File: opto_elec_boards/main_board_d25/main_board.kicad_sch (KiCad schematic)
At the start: 28 parts, among them J1 IN1_BNC, J10 To Slave Board, J11 SWITCH_B, J12 SWITCH_C, J13 DB25_Socket_MountingHoles, J2 IN2_BNC, J3 OUT1_BNC, J4 OUT2_BNC, J5 OUT3_BNC, J6 OUT4_BNC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

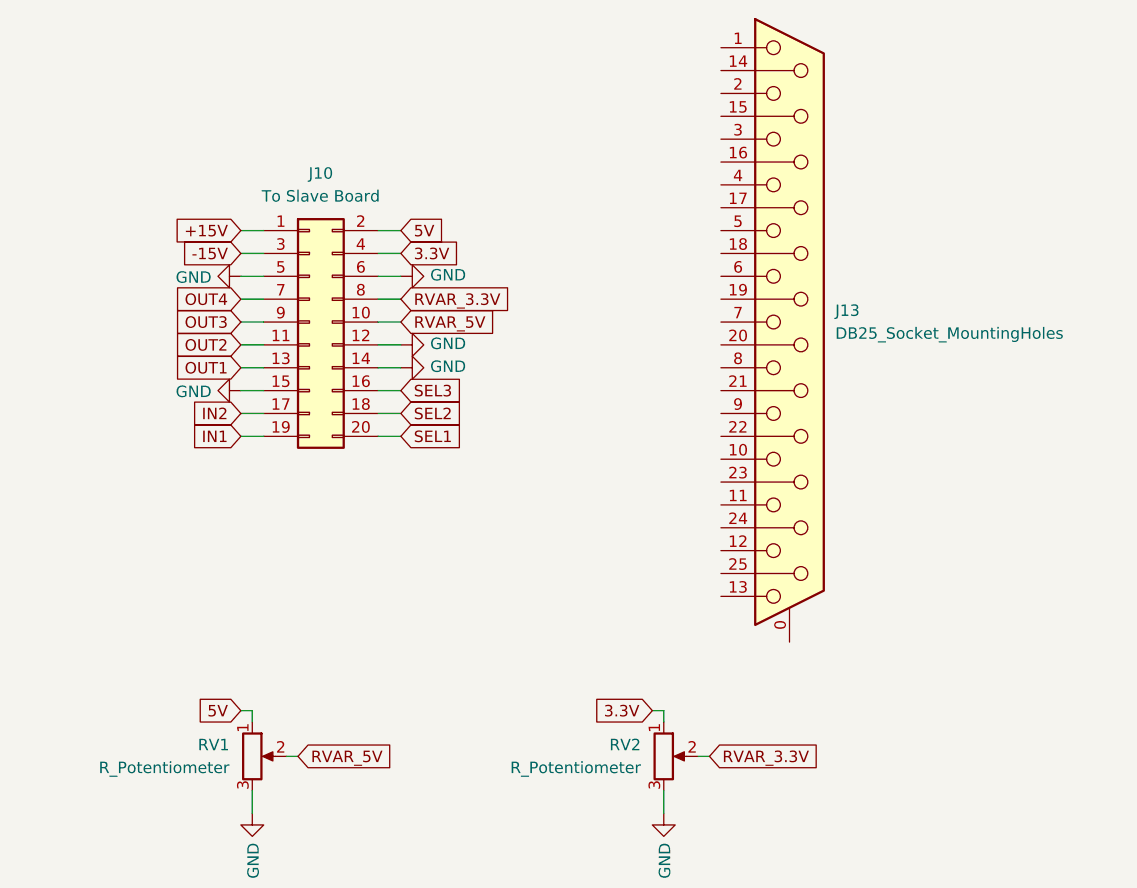
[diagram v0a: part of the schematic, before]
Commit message: Create Opto Board Main D25 / new connector test
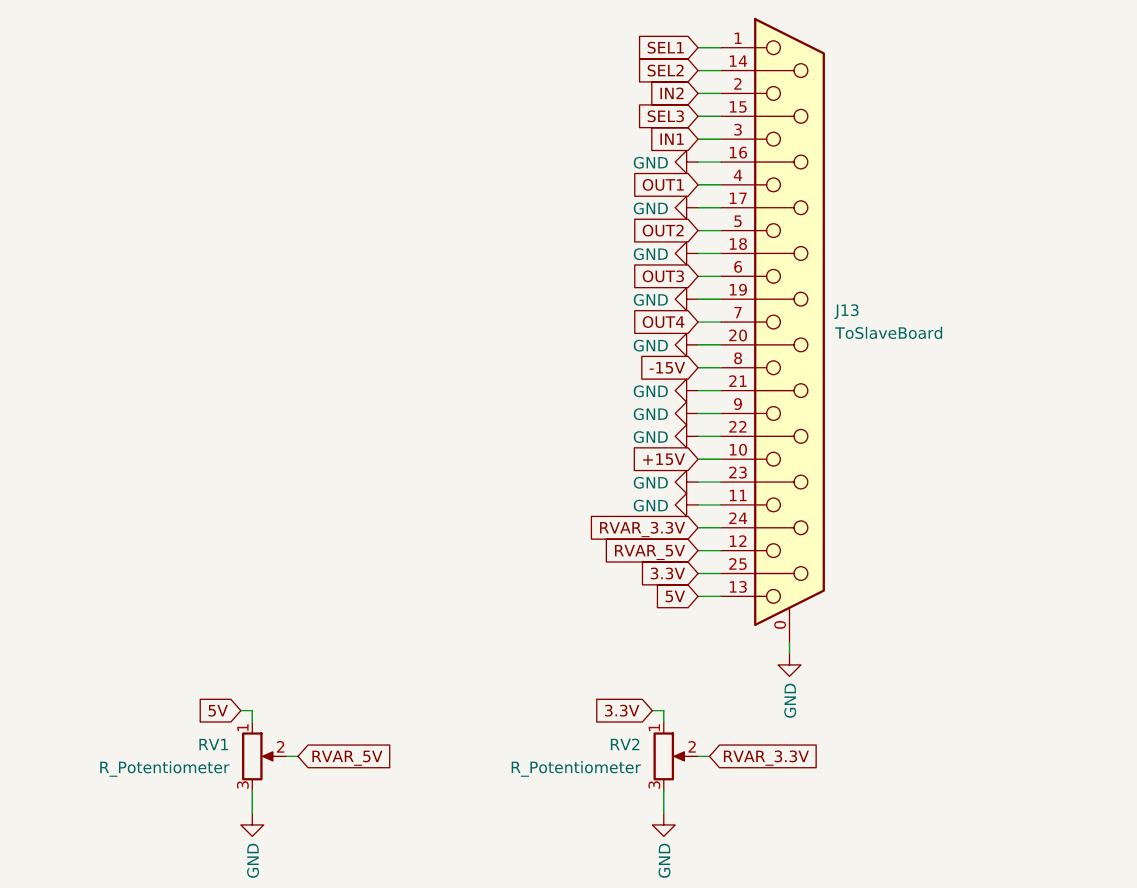
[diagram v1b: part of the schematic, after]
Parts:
- removed J10: To Slave Board, Connector_PinSocket_2.54mm:PinSocket_2x10_P2.54mm_Horizontal, symbol Connector_Generic:Conn_02x10_Odd_Even
- J13: value DB25_Socket_MountingHoles -> ToSlaveBoard
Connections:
- net +15V: now also J13.10
- net -15V: now also J13.8
- net 3.3V: now also J13.25 (P25)
- net 5V: now also J13.13
- net GND: now also J13.0 (PAD), J13.11, J13.16 (P16), J13.17 (P17), J13.18 (P18), J13.19 (P19), J13.20 (P20), J13.21 (P21), J13.22 (P22), J13.23 (P23), J13.9
- net IN1: now also J13.3
- net IN2: now also J13.2
- net OUT1: now also J13.4
- net OUT2: now also J13.5
- net OUT3: now also J13.6
- net OUT4: now also J13.7
- net RVAR_3.3V: now also J13.24 (P24)
- net RVAR_5V: now also J13.12
- net SEL1: now also J13.1
- net SEL2: now also J13.14 (P14)
- net SEL3: now also J13.15 (P15)

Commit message: Update OptoBoard / D25 version
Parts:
- added RV3: R_Potentiometer, Connector_PinHeader_2.54mm:PinHeader_1x03_P2.54mm_Vertical, symbol Device:R_Potentiometer
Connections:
- net +15V: now also RV3.1
- net GND: now also RV3.3; no longer J13.11
- new net RVAR_15V: J13.11, RV3.2
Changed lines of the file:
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@@
 	(wire
 		(pts
+			(xy 172.72 74.93) (xy 172.72 77.47)
+		)
+		(stroke
+			(width 0)
+			(type default)
+		)
+	)
+	(wire
+		(pts
 			(xy 90.17 81.28) (xy 90.17 78.74)
 		)
@@
 	(wire
 		(pts
+			(xy 171.45 66.04) (xy 172.72 66.04)
+		)
+		(stroke
+			(width 0)
+			(type default)
+		)
+	)
+	(wire
+		(pts
 			(xy 224.79 132.08) (xy 224.79 139.7)
 		)
@@
 	(wire
 		(pts
+			(xy 176.53 71.12) (xy 177.8 71.12)
+		)
+		(stroke
+			(width 0)
+			(type default)
+		)
+	)
+	(wire
+		(pts
 			(xy 45.72 95.25) (xy 45.72 92.71)
 		)
@@
 	(wire
 		(pts
+			(xy 172.72 66.04) (xy 172.72 67.31)
+		)
+		(stroke
+			(width 0)
+			(type default)
+		)
+	)
+	(wire
+		(pts
 			(xy 194.31 139.7) (xy 196.85 139.7)
 		)
@@
 	(global_label "+15V"
 		(shape input)
+		(at 171.45 66.04 180)
+		(effects
+			(font
+				(size 1.27 1.27)
+			)
+			(justify right)
+		)
+		(property "Intersheetrefs" "${INTERSHEET_REFS}"
+			(at 171.45 66.04 0)
+			(effects
+				(font
+					(size 1.27 1.27)
+				)
+				(hide yes)
+			)
+		)
+	)
+	(global_label "+15V"
+		(shape input)
 		(at 85.09 43.18 0)
 		(effects
@@
 		)
 	)
+	(global_label "RVAR_15V"
+		(shape input)
+		(at 222.25 73.66 180)
+		(effects
+			(font
+				(size 1.27 1.27)
+			)
+			(justify right)
+		)
+		(property "Intersheetrefs" "${INTERSHEET_REFS}"
+			(at 222.25 73.66 0)
+			(effects
+				(font
+					(size 1.27 1.27)
+				)
+				(hide yes)
+			)
+		)
+	)
 	(global_label "OUT2"
 		(shape input)
@@
 		)
 	)
+	(global_label "RVAR_15V"
+		(shape input)
+		(at 177.8 71.12 0)
+		(effects
+			(font
+				(size 1.27 1.27)
+			)
+			(justify left)
+		)
+		(property "Intersheetrefs" "${INTERSHEET_REFS}"
+			(at 177.8 71.12 0)
+			(effects
+				(font
+					(size 1.27 1.27)
+				)
+				(hide yes)
+			)
+		)
+	)
 	(global_label "3.3V"
 		(shape input)
@@
 	)
 	(symbol
-		(lib_id "power:GND")
-		(at 222.25 73.66 270)
-		(unit 1)
-		(exclude_from_sim no)
-		(in_bom yes)
-		(on_board yes)
-		(dnp no)
-		(property "Reference" "#PWR0110"
-			(at 215.9 73.66 0)
-			(effects
-				(font
-					(size 1.27 1.27)
-				)
-				(hide yes)
-			)
-		)
-		(property "Value" "GND"
-			(at 218.9988 73.787 90)
-			(effects
-				(font
-					(size 1.27 1.27)
-				)
-				(justify right)
-			)
-		)
-		(property "Footprint" ""
-			(at 222.25 73.66 0)
-			(effects
-				(font
-					(size 1.27 1.27)
-				)
-				(hide yes)
-			)
-		)
-		(property "Datasheet" ""
-			(at 222.25 73.66 0)
-			(effects
-				(font
-					(size 1.27 1.27)
-				)
-				(hide yes)
-			)
-		)
-		(property "Description" ""
-			(at 222.25 73.66 0)
-			(effects
-				(font
-					(size 1.27 1.27)
-				)
-			)
-		)
-		(pin "1"
-		)
-		(instances
-			(project ""
-				(path "/57df33c0-6f05-4aba-b5b1-deb15b1b9db6"
-					(reference "#PWR0110")
-					(unit 1)
-				)
-			)
-		)
-	)
-	(symbol
 		(lib_id "Regulator_Linear:L7805")
 		(at 104.14 78.74 0)
@@
 	(symbol
 		(lib_id "power:GND")
+		(at 172.72 77.47 0)
+		(unit 1)
+		(exclude_from_sim no)
+		(in_bom yes)
+		(on_board yes)
+		(dnp no)
+		(property "Reference" "#PWR016"
+			(at 172.72 83.82 0)
+			(effects
+				(font
+					(size 1.27 1.27)
+				)
+				(hide yes)
+			)
+		)
+		(property "Value" "GND"
+			(at 172.847 80.7212 90)
+			(effects
+				(font
+					(size 1.27 1.27)
+				)
+				(justify right)
+			)
+		)
+		(property "Footprint" ""
+			(at 172.72 77.47 0)
+			(effects
+				(font
+					(size 1.27 1.27)
+				)
+				(hide yes)
+			)
+		)
+		(property "Datasheet" ""
+			(at 172.72 77.47 0)
+			(effects
+				(font
+					(size 1.27 1.27)
+				)
+				(hide yes)
+			)
+		)
+		(property "Description" ""
+			(at 172.72 77.47 0)
+			(effects
+				(font
+					(size 1.27 1.27)
+				)
+			)
+		)
+		(pin "1"
+		)
+		(instances
+			(project "main_board"
+				(path "/57df33c0-6f05-4aba-b5b1-deb15b1b9db6"
+					(reference "#PWR016")
+					(unit 1)
+				)
+			)
+		)
+	)
+	(symbol
+		(lib_id "power:GND")
 		(at 232.41 90.17 0)
 		(unit 1)
@@
 					(unit 1)
 				)
+			)
+		)
+	)
+	(symbol
+		(lib_id "Device:R_Potentiometer")
+		(at 172.72 71.12 0)
+		(unit 1)
+		(exclude_from_sim no)
+		(in_bom yes)
+		(on_board yes)
+		(dnp no)
+		(fields_autoplaced yes)
+		(property "Reference" "RV3"
+			(at 170.18 69.8499 0)
+			(effects
+				(font
+					(size 1.27 1.27)
+				)
+				(justify right)
+			)
+		)
+		(property "Value" "R_Potentiometer"
+			(at 170.18 72.3899 0)
+			(effects
+				(font
+					(size 1.27 1.27)
+				)
+				(justify right)
+			)
+		)
+		(property "Footprint" "Connector_PinHeader_2.54mm:PinHeader_1x03_P2.54mm_Vertical"
+			(at 172.72 71.12 0)
+			(effects
+				(font
+					(size 1.27 1.27)
+				)
+				(hide yes)
+			)
+		)
+		(property "Datasheet" "~"
+			(at 172.72 71.12 0)
+			(effects
+				(font
+					(size 1.27 1.27)
+				)
+				(hide yes)
+			)
+		)
+		(property "Description" "Potentiometer"
+			(at 172.72 71.12 0)
+			(effects
+				(font
+					(size 1.27 1.27)
+				)
+				(hide yes)
+			)
+		)
+		(pin "1"
+		)
+		(pin "3"
+		)
+		(pin "2"
+		)
+		(instances
+			(project "main_board"
+				(path "/57df33c0-6f05-4aba-b5b1-deb15b1b9db6"
+					(reference "RV3")
+					(unit 1)
+				)

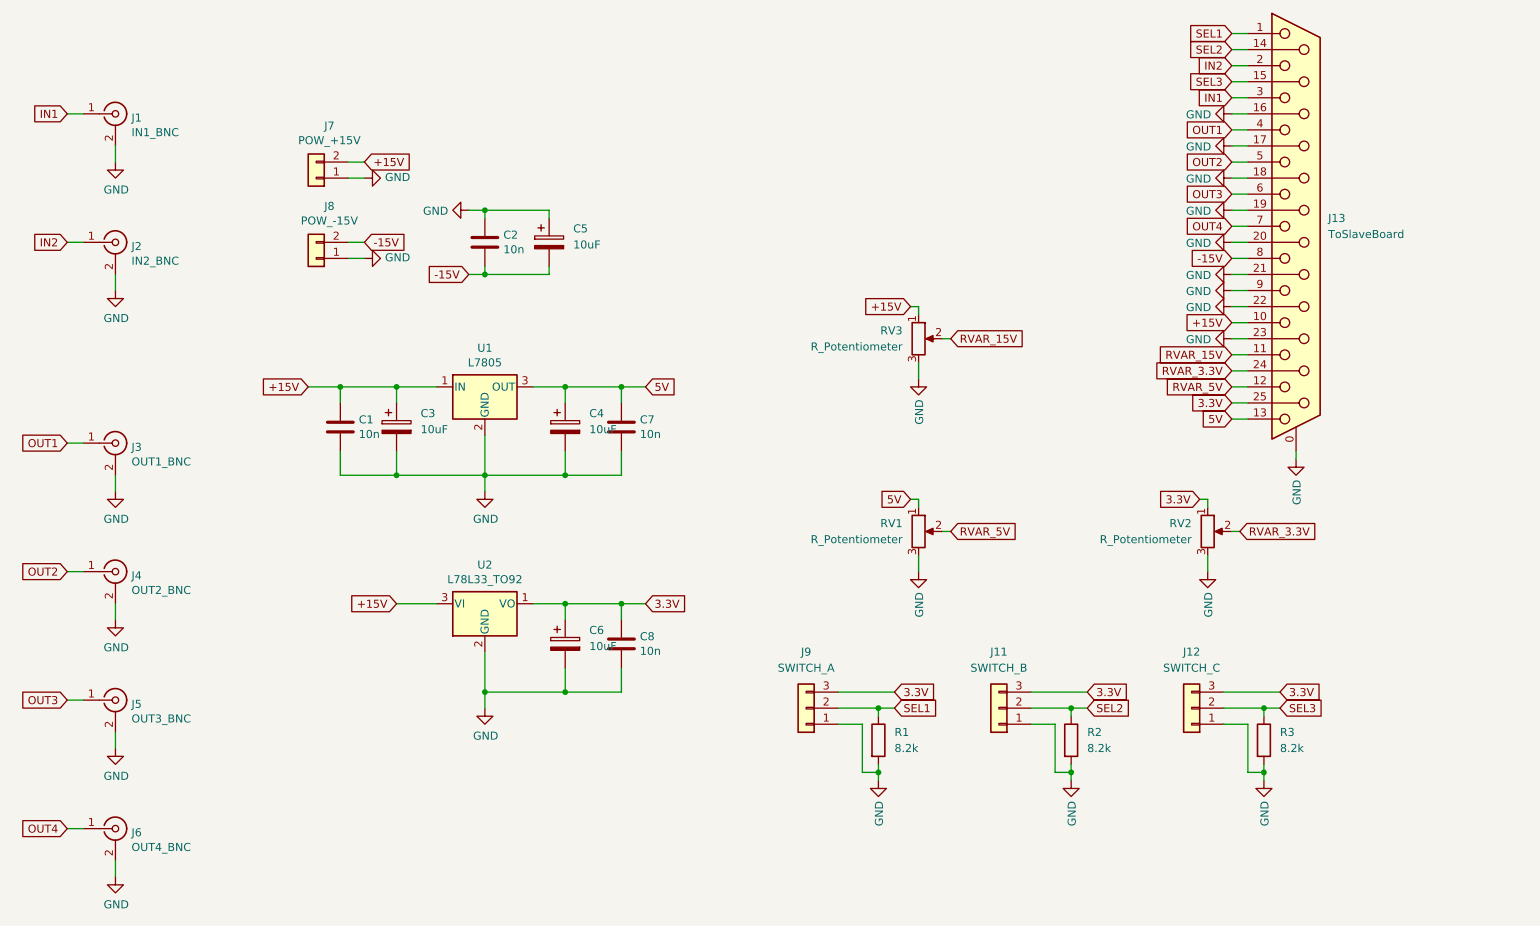
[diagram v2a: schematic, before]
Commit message: Update Opto / Master and PhD Slave boards
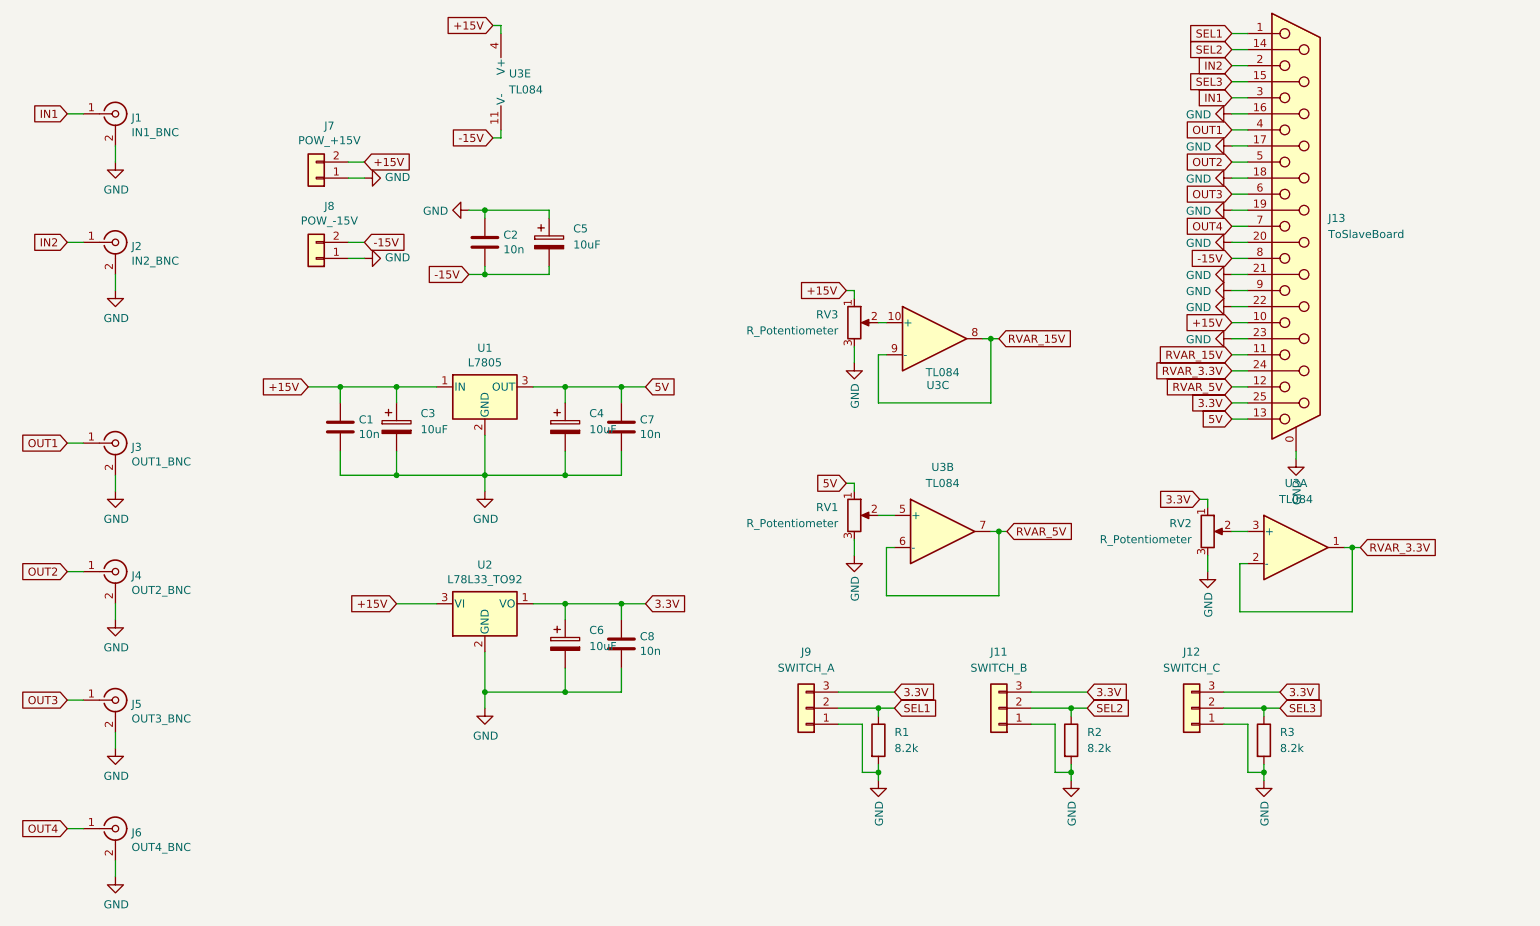
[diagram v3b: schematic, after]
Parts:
- added U3: TL084, Package_DIP:DIP-14_W7.62mm_Socket_LongPads, symbol Amplifier_Operational:TL084
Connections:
- net +15V: now also U3.4 (V+)
- net -15V: now also U3.11 (V-)
- net RVAR_15V: now also U3.8, U3.9 (-); no longer RV3.2
- net RVAR_3.3V: now also U3.1, U3.2 (-); no longer RV2.2
- net RVAR_5V: now also U3.6 (-), U3.7; no longer RV1.2
- new net: RV3.2, U3.10 (+)
- new net: RV2.2, U3.3 (+)
- new net: RV1.2, U3.5 (+)
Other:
- moved on the sheet: RV1, RV3
